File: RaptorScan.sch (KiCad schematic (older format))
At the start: 1 part

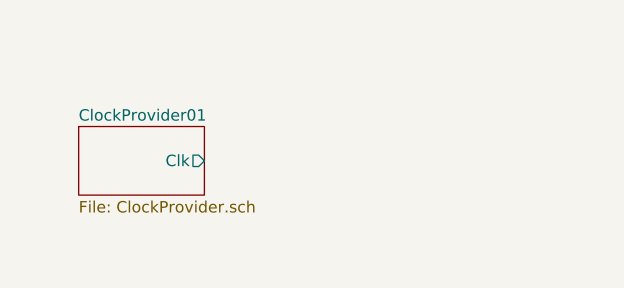
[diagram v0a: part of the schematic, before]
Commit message: Added: 7 Bit Counter
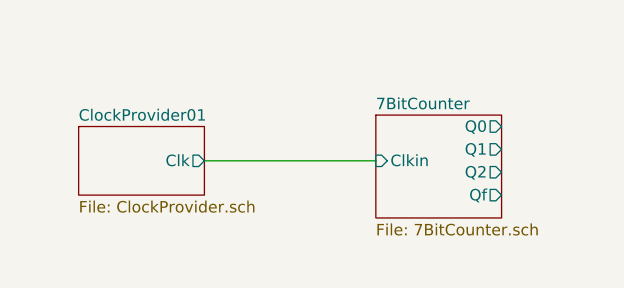
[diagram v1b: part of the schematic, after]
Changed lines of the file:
@@
 EESchema Schematic File Version 4
+LIBS:RaptorScan-cache
 EELAYER 29 0
 EELAYER END
 $Descr A4 11693 8268
 encoding utf-8
-Sheet 1 2
+Sheet 1 3
 Title ""
 Date ""
@@
 F0 "ClockProvider01" 50
 F1 "ClockProvider.sch" 50
-F4 "Clk" O R 2550 1100 50
+F2 "Clk" O R 2550 1100 50
 $EndSheet
 Wire Wire Line
@@
 	1    0    0    -1
 $EndComp
+$Sheet
+S 3300 900  550  450
+U 5D12D5A5
+F0 "7BitCounter" 50
+F1 "7BitCounter.sch" 50
+F2 "Clkin" I L 3300 1100 50
+F3 "Q0" O R 3850 950 50
+F4 "Q1" O R 3850 1050 50
+F5 "Q2" O R 3850 1150 50
+F6 "Qf" O R 3850 1250 50
+$EndSheet
+Wire Wire Line
+	2550 1100 3300 1100
 $EndSCHEMATC

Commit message: Update
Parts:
- added D1, D2, D3: LED, symbol Device:LED
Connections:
- net GND: now also D1.1 (K), D2.1 (K), D3.1 (K)
- new net MuxDecoder/A: D1.2 (A)
- new net MuxDecoder/B: D2.2 (A)
- new net MuxDecoder/C: D3.2 (A)
- no-connect marks 0 -> 4
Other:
- moved on the sheet: BT1
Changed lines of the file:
@@
 $Descr A4 11693 8268
 encoding utf-8
-Sheet 1 3
+Sheet 1 4
 Title ""
 Date ""
@@
 $EndDescr
 $Sheet
-S 2000 950  550  300
+S 2300 950  550  300
 U 5D1172DE
 F0 "ClockProvider01" 50
 F1 "ClockProvider.sch" 50
-F2 "Clk" O R 2550 1100 50
+F2 "Clk" O R 2850 1100 50
 $EndSheet
 Wire Wire Line
-	1100 700  1100 750
+	1500 800  1500 850
 $Comp
 L power:+12V #PWR0102
 U 1 1 5D1362F3
-P 1100 700
-F 0 "#PWR0102" H 1100 550 50  0001 C CNN
-F 1 "+12V" H 1115 873 50  0000 C CNN
-F 2 "" H 1100 700 50  0001 C CNN
-F 3 "" H 1100 700 50  0001 C CNN
-	1    1100 700
+P 1500 800
+F 0 "#PWR0102" H 1500 650 50  0001 C CNN
+F 1 "+12V" H 1515 973 50  0000 C CNN
+F 2 "" H 1500 800 50  0001 C CNN
+F 3 "" H 1500 800 50  0001 C CNN
+	1    1500 800
 	1    0    0    -1
 $EndComp
@@
 L power:GND #PWR0103
 U 1 1 5D137CC7
-P 1100 1350
-F 0 "#PWR0103" H 1100 1100 50  0001 C CNN
-F 1 "GND" H 1105 1177 50  0000 C CNN
-F 2 "" H 1100 1350 50  0001 C CNN
-F 3 "" H 1100 1350 50  0001 C CNN
-	1    1100 1350
-	1    0    0    -1
-$EndComp
-Wire Wire Line
-	1100 1250 1100 1300
+P 1500 1450
+F 0 "#PWR0103" H 1500 1200 50  0001 C CNN
+F 1 "GND" H 1505 1277 50  0000 C CNN
+F 2 "" H 1500 1450 50  0001 C CNN
+F 3 "" H 1500 1450 50  0001 C CNN
+	1    1500 1450
+	1    0    0    -1
+$EndComp
+Wire Wire Line
+	1500 1350 1500 1400
 $Comp
 L power:PWR_FLAG #FLG0101
 U 1 1 5D13C6DB
-P 1100 750
-F 0 "#FLG0101" H 1100 825 50  0001 C CNN
-F 1 "PWR_FLAG" V 1100 878 50  0000 L CNN
-F 2 "" H 1100 750 50  0001 C CNN
-F 3 "~" H 1100 750 50  0001 C CNN
-	1    1100 750
+P 1500 850
+F 0 "#FLG0101" H 1500 925 50  0001 C CNN
+F 1 "PWR_FLAG" V 1500 978 50  0000 L CNN
+F 2 "" H 1500 850 50  0001 C CNN
+F 3 "~" H 1500 850 50  0001 C CNN
+	1    1500 850
 	0    1    1    0
 $EndComp
-Connection ~ 1100 750
-Wire Wire Line
-	1100 750  1100 850
+Connection ~ 1500 850
+Wire Wire Line
+	1500 850  1500 950
 $Comp
 L power:PWR_FLAG #FLG0102
 U 1 1 5D13CBD4
-P 1100 1300
-F 0 "#FLG0102" H 1100 1375 50  0001 C CNN
-F 1 "PWR_FLAG" V 1100 1428 50  0000 L CNN
-F 2 "" H 1100 1300 50  0001 C CNN
-F 3 "~" H 1100 1300 50  0001 C CNN
-	1    1100 1300
+P 1500 1400
+F 0 "#FLG0102" H 1500 1475 50  0001 C CNN
+F 1 "PWR_FLAG" V 1500 1528 50  0000 L CNN
+F 2 "" H 1500 1400 50  0001 C CNN
+F 3 "~" H 1500 1400 50  0001 C CNN
+	1    1500 1400
 	0    1    1    0
 $EndComp
-Connection ~ 1100 1300
-Wire Wire Line
-	1100 1300 1100 1350
+Connection ~ 1500 1400
+Wire Wire Line
+	1500 1400 1500 1450
 $Comp
 L Device:Battery BT1
 U 1 1 5D11AF0F
-P 1100 1050
-F 0 "BT1" H 1208 1096 50  0000 L CNN
-F 1 "12V" H 1208 1005 50  0000 L CNN
-F 2 "" V 1100 1110 50  0001 C CNN
-F 3 "~" V 1100 1110 50  0001 C CNN
-	1    1100 1050
+P 1500 1150
+F 0 "BT1" H 1608 1196 50  0000 L CNN
+F 1 "12V" H 1608 1105 50  0000 L CNN
+F 2 "" V 1500 1210 50  0001 C CNN
+F 3 "~" V 1500 1210 50  0001 C CNN
+	1    1500 1150
 	1    0    0    -1
 $EndComp
 $Sheet
-S 3300 900  550  450
+S 4300 1050 550  700
 U 5D12D5A5
 F0 "7BitCounter" 50
 F1 "7BitCounter.sch" 50
-F2 "Clkin" I L 3300 1100 50
-F3 "Q0" O R 3850 950 50
-F4 "Q1" O R 3850 1050 50
-F5 "Q2" O R 3850 1150 50
-F6 "Qf" O R 3850 1250 50
+F2 "Clkin" I L 4300 1100 50
+F3 "Q0" O L 4300 1400 50
+F4 "Q1" O L 4300 1500 50
+F5 "Q2" O L 4300 1600 50
+F6 "Q3" O L 4300 1700 50
+F7 "Q4" O R 4850 1700 50
+F8 "Q5" O R 4850 1600 50
+F9 "Q6" O R 4850 1500 50
 $EndSheet
-Wire Wire Line
-	2550 1100 3300 1100
+$Sheet
+S 3200 1050 800  600
+U 5D12D28E
+F0 "MuxDecoder" 50
+F1 "MuxDecoder.sch" 50
+F2 "A" O L 3200 1400 50
+F3 "B" O L 3200 1500 50
+F4 "C" O L 3200 1600 50
+F5 "X" I R 4000 1400 50
+F6 "Y" I R 4000 1500 50
+F7 "Z" I R 4000 1600 50
+F8 "Clkin" I L 3200 1100 50
+F9 "ClkOut" O R 4000 1100 50
+$EndSheet
+Wire Wire Line
+	4300 1400 4000 1400
+Wire Wire Line
+	4300 1500 4000 1500
+Wire Wire Line
+	4300 1600 4000 1600
+NoConn ~ 4300 1700
+Wire Wire Line
+	2850 1100 3200 1100
+Wire Wire Line
+	4000 1100 4300 1100
+NoConn ~ 4850 1500
+NoConn ~ 4850 1600
+NoConn ~ 4850 1700
+$Comp
+L Device:LED D1
+U 1 1 5D23D3BD
+P 2550 1600
+F 0 "D1" H 2543 1816 50  0000 C CNN
+F 1 "LED" H 2543 1725 50  0000 C CNN
+F 2 "" H 2550 1600 50  0001 C CNN
+F 3 "~" H 2550 1600 50  0001 C CNN
+	1    2550 1600
+	1    0    0    -1
+$EndComp
+$Comp
+L Device:LED D2
+U 1 1 5D23E2F8
+P 2550 1950
+F 0 "D2" H 2543 2166 50  0000 C CNN
+F 1 "LED" H 2543 2075 50  0000 C CNN
+F 2 "" H 2550 1950 50  0001 C CNN
+F 3 "~" H 2550 1950 50  0001 C CNN
+	1    2550 1950
+	1    0    0    -1
+$EndComp
+$Comp
+L Device:LED D3
+U 1 1 5D23E6C2
+P 2550 2300
+F 0 "D3" H 2543 2516 50  0000 C CNN
+F 1 "LED" H 2543 2425 50  0000 C CNN
+F 2 "" H 2550 2300 50  0001 C CNN
+F 3 "~" H 2550 2300 50  0001 C CNN
+	1    2550 2300
+	1    0    0    -1
+$EndComp
+Wire Wire Line
+	2700 1600 2900 1600
+Wire Wire Line
+	2900 1600 2900 1400
+Wire Wire Line
+	2900 1400 3200 1400
+Wire Wire Line
+	3200 1500 3000 1500
+Wire Wire Line
+	3000 1500 3000 1950
+Wire Wire Line
+	3000 1950 2700 1950
+Wire Wire Line
+	3200 1600 3100 1600
+Wire Wire Line
+	3100 1600 3100 2300
+Wire Wire Line
+	3100 2300 2700 2300
+Wire Wire Line
+	2400 2300 2200 2300
+Wire Wire Line
+	2200 2300 2200 1950
+Wire Wire Line
+	2200 1600 2400 1600
+Wire Wire Line
+	2400 1950 2200 1950
+Connection ~ 2200 1950
+Wire Wire Line
+	2200 1950 2200 1600
+$Comp
+L power:GND #PWR0104
+U 1 1 5D23FAED
+P 2200 2300
+F 0 "#PWR0104" H 2200 2050 50  0001 C CNN
+F 1 "GND" H 2205 2127 50  0000 C CNN
+F 2 "" H 2200 2300 50  0001 C CNN
+F 3 "" H 2200 2300 50  0001 C CNN
+	1    2200 2300
+	1    0    0    -1
+$EndComp
+Connection ~ 2200 2300
 $EndSCHEMATC

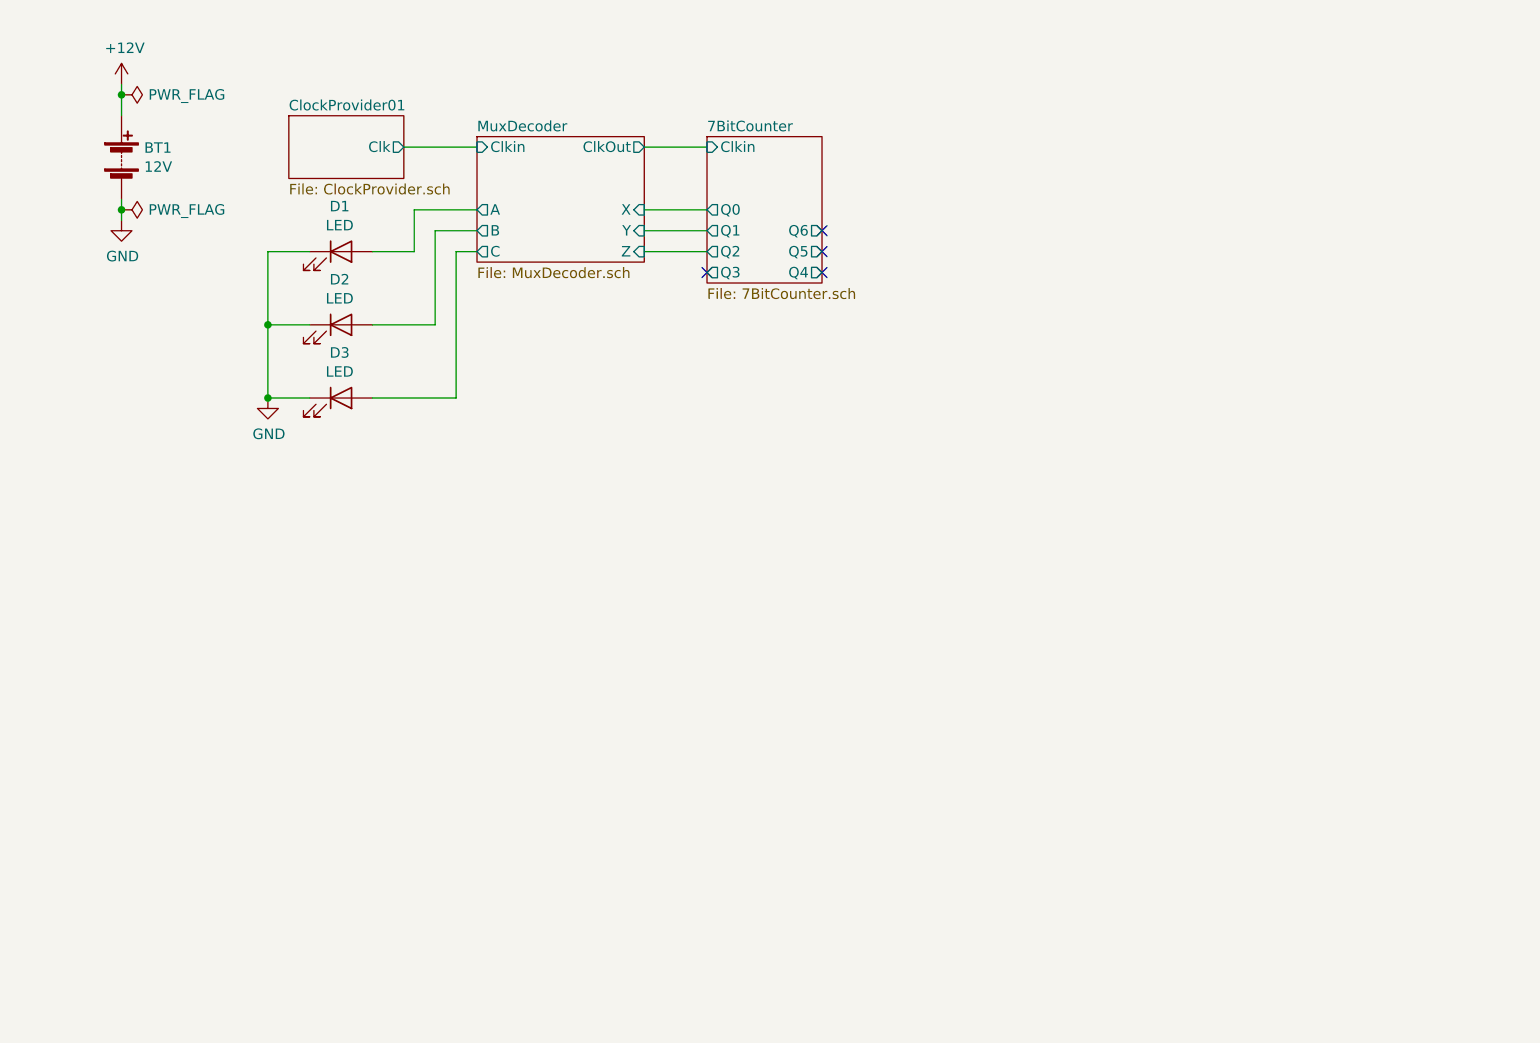
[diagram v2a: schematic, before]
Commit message: Added: connectors
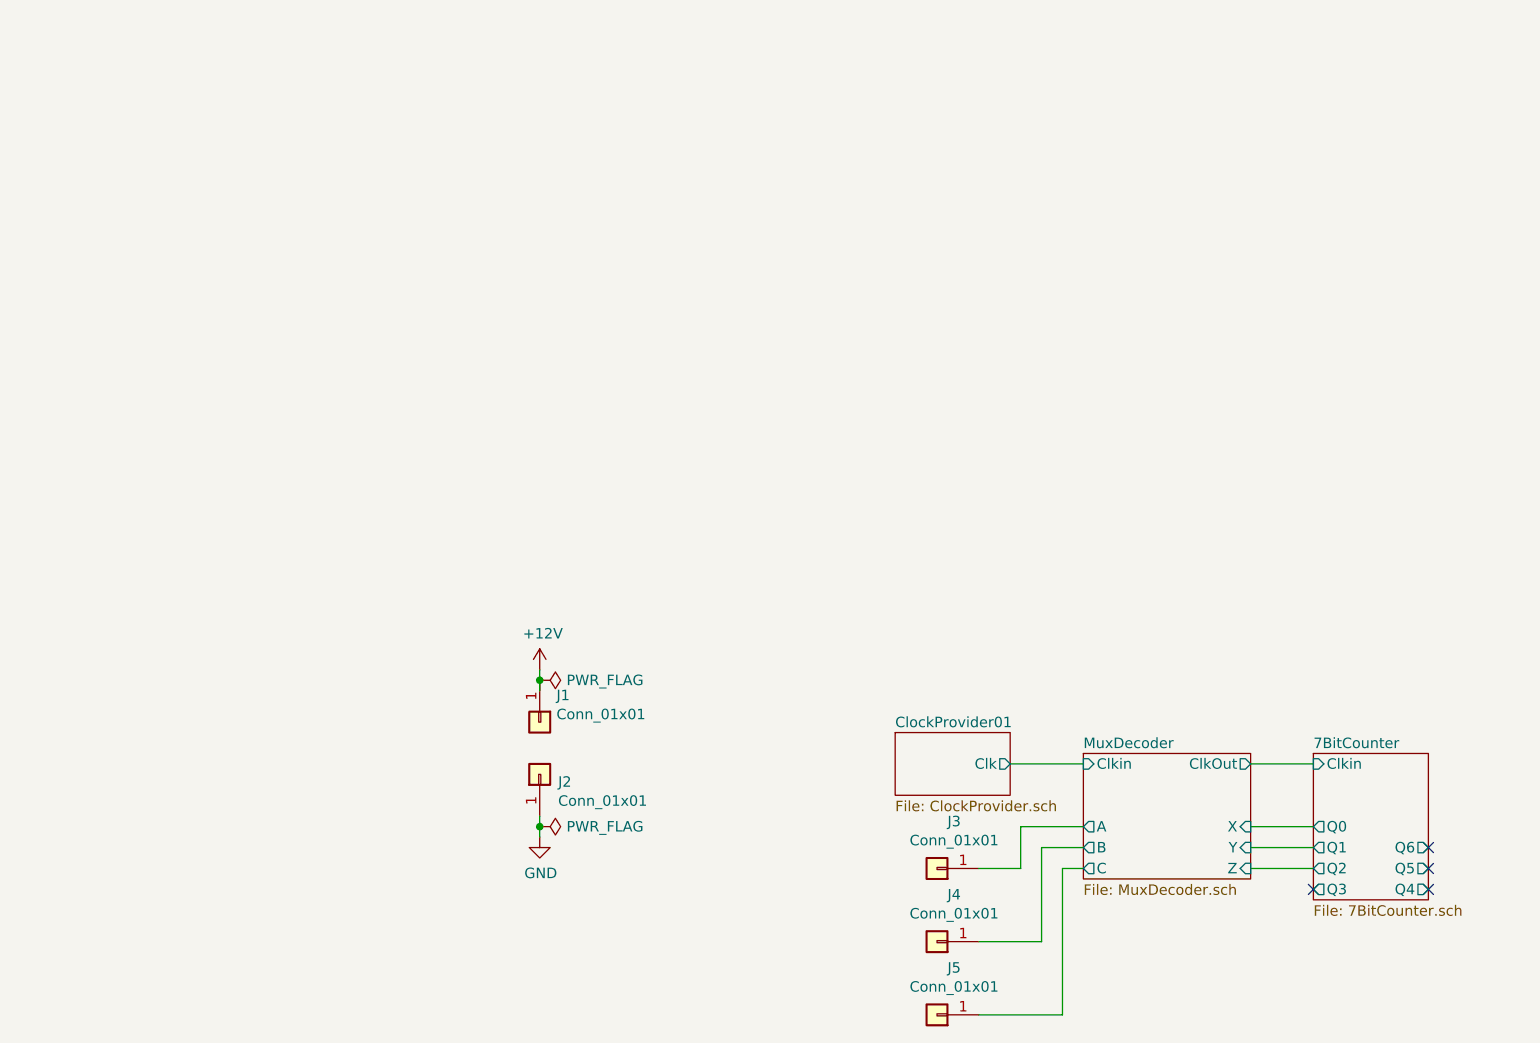
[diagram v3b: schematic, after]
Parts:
- removed BT1: 12V, symbol Device:Battery
- removed D1, D2, D3: LED, symbol Device:LED
- added J1, J2, J3, J4, J5: Conn_01x01, symbol Connector_Generic:Conn_01x01
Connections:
- wire segments 23 -> 18
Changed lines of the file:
@@
 $EndDescr
 $Sheet
-S 2300 950  550  300
+S 5200 3900 550  300
 U 5D1172DE
 F0 "ClockProvider01" 50
 F1 "ClockProvider.sch" 50
-F2 "Clk" O R 2850 1100 50
+F2 "Clk" O R 5750 4050 50
 $EndSheet
 Wire Wire Line
-	1500 800  1500 850
+	3500 3600 3500 3650
 $Comp
 L power:+12V #PWR0102
 U 1 1 5D1362F3
-P 1500 800
-F 0 "#PWR0102" H 1500 650 50  0001 C CNN
-F 1 "+12V" H 1515 973 50  0000 C CNN
-F 2 "" H 1500 800 50  0001 C CNN
-F 3 "" H 1500 800 50  0001 C CNN
-	1    1500 800
+P 3500 3600
+F 0 "#PWR0102" H 3500 3450 50  0001 C CNN
+F 1 "+12V" H 3515 3773 50  0000 C CNN
+F 2 "" H 3500 3600 50  0001 C CNN
+F 3 "" H 3500 3600 50  0001 C CNN
+	1    3500 3600
 	1    0    0    -1
 $EndComp
@@
 L power:GND #PWR0103
 U 1 1 5D137CC7
-P 1500 1450
-F 0 "#PWR0103" H 1500 1200 50  0001 C CNN
-F 1 "GND" H 1505 1277 50  0000 C CNN
-F 2 "" H 1500 1450 50  0001 C CNN
-F 3 "" H 1500 1450 50  0001 C CNN
-	1    1500 1450
+P 3500 4400
+F 0 "#PWR0103" H 3500 4150 50  0001 C CNN
+F 1 "GND" H 3505 4227 50  0000 C CNN
+F 2 "" H 3500 4400 50  0001 C CNN
+F 3 "" H 3500 4400 50  0001 C CNN
+	1    3500 4400
 	1    0    0    -1
 $EndComp
 Wire Wire Line
-	1500 1350 1500 1400
+	3500 4300 3500 4350
 $Comp
 L power:PWR_FLAG #FLG0101
 U 1 1 5D13C6DB
-P 1500 850
-F 0 "#FLG0101" H 1500 925 50  0001 C CNN
-F 1 "PWR_FLAG" V 1500 978 50  0000 L CNN
-F 2 "" H 1500 850 50  0001 C CNN
-F 3 "~" H 1500 850 50  0001 C CNN
-	1    1500 850
+P 3500 3650
+F 0 "#FLG0101" H 3500 3725 50  0001 C CNN
+F 1 "PWR_FLAG" V 3500 3778 50  0000 L CNN
+F 2 "" H 3500 3650 50  0001 C CNN
+F 3 "~" H 3500 3650 50  0001 C CNN
+	1    3500 3650
 	0    1    1    0
 $EndComp
-Connection ~ 1500 850
+Connection ~ 3500 3650
 Wire Wire Line
-	1500 850  1500 950
+	3500 3650 3500 3700
 $Comp
 L power:PWR_FLAG #FLG0102
 U 1 1 5D13CBD4
-P 1500 1400
-F 0 "#FLG0102" H 1500 1475 50  0001 C CNN
-F 1 "PWR_FLAG" V 1500 1528 50  0000 L CNN
-F 2 "" H 1500 1400 50  0001 C CNN
-F 3 "~" H 1500 1400 50  0001 C CNN
-	1    1500 1400
+P 3500 4350
+F 0 "#FLG0102" H 3500 4425 50  0001 C CNN
+F 1 "PWR_FLAG" V 3500 4478 50  0000 L CNN
+F 2 "" H 3500 4350 50  0001 C CNN
+F 3 "~" H 3500 4350 50  0001 C CNN
+	1    3500 4350
 	0    1    1    0
 $EndComp
-Connection ~ 1500 1400
+Connection ~ 3500 4350
 Wire Wire Line
-	1500 1400 1500 1450
-$Comp
-L Device:Battery BT1
-U 1 1 5D11AF0F
-P 1500 1150
-F 0 "BT1" H 1608 1196 50  0000 L CNN
-F 1 "12V" H 1608 1105 50  0000 L CNN
-F 2 "" V 1500 1210 50  0001 C CNN
-F 3 "~" V 1500 1210 50  0001 C CNN
-	1    1500 1150
-	1    0    0    -1
-$EndComp
+	3500 4350 3500 4400
 $Sheet
-S 4300 1050 550  700
+S 7200 4000 550  700
 U 5D12D5A5
 F0 "7BitCounter" 50
 F1 "7BitCounter.sch" 50
-F2 "Clkin" I L 4300 1100 50
-F3 "Q0" O L 4300 1400 50
-F4 "Q1" O L 4300 1500 50
-F5 "Q2" O L 4300 1600 50
-F6 "Q3" O L 4300 1700 50
-F7 "Q4" O R 4850 1700 50
-F8 "Q5" O R 4850 1600 50
-F9 "Q6" O R 4850 1500 50
+F2 "Clkin" I L 7200 4050 50
+F3 "Q0" O L 7200 4350 50
+F4 "Q1" O L 7200 4450 50
+F5 "Q2" O L 7200 4550 50
+F6 "Q3" O L 7200 4650 50
+F7 "Q4" O R 7750 4650 50
+F8 "Q5" O R 7750 4550 50
+F9 "Q6" O R 7750 4450 50
 $EndSheet
 $Sheet
-S 3200 1050 800  600
+S 6100 4000 800  600
 U 5D12D28E
 F0 "MuxDecoder" 50
 F1 "MuxDecoder.sch" 50
-F2 "A" O L 3200 1400 50
-F3 "B" O L 3200 1500 50
-F4 "C" O L 3200 1600 50
-F5 "X" I R 4000 1400 50
-F6 "Y" I R 4000 1500 50
-F7 "Z" I R 4000 1600 50
-F8 "Clkin" I L 3200 1100 50
-F9 "ClkOut" O R 4000 1100 50
+F2 "A" O L 6100 4350 50
+F3 "B" O L 6100 4450 50
+F4 "C" O L 6100 4550 50
+F5 "X" I R 6900 4350 50
+F6 "Y" I R 6900 4450 50
+F7 "Z" I R 6900 4550 50
+F8 "Clkin" I L 6100 4050 50
+F9 "ClkOut" O R 6900 4050 50
 $EndSheet
 Wire Wire Line
-	4300 1400 4000 1400
+	7200 4350 6900 4350
 Wire Wire Line
-	4300 1500 4000 1500
+	7200 4450 6900 4450
 Wire Wire Line
-	4300 1600 4000 1600
-NoConn ~ 4300 1700
+	7200 4550 6900 4550
+NoConn ~ 7200 4650
 Wire Wire Line
-	2850 1100 3200 1100
+	5750 4050 6100 4050
 Wire Wire Line
-	4000 1100 4300 1100
-NoConn ~ 4850 1500
-NoConn ~ 4850 1600
-NoConn ~ 4850 1700
+	6900 4050 7200 4050
+NoConn ~ 7750 4450
+NoConn ~ 7750 4550
+NoConn ~ 7750 4650
+Wire Wire Line
+	5600 4550 5800 4550
+Wire Wire Line
+	5800 4550 5800 4350
+Wire Wire Line
+	5800 4350 6100 4350
+Wire Wire Line
+	6100 4450 5900 4450
+Wire Wire Line
+	5900 4450 5900 4900
+Wire Wire Line
+	5900 4900 5600 4900
+Wire Wire Line
+	6100 4550 6000 4550
+Wire Wire Line
+	6000 4550 6000 5250
+Wire Wire Line
+	6000 5250 5600 5250
 $Comp
-L Device:LED D1
-U 1 1 5D23D3BD
-P 2550 1600
-F 0 "D1" H 2543 1816 50  0000 C CNN
-F 1 "LED" H 2543 1725 50  0000 C CNN
-F 2 "" H 2550 1600 50  0001 C CNN
-F 3 "~" H 2550 1600 50  0001 C CNN
-	1    2550 1600
-	1    0    0    -1
+L Connector_Generic:Conn_01x01 J1
+U 1 1 5D13F6A9
+P 3500 3850
+F 0 "J1" V 3372 3930 50  0000 L CNN
+F 1 "Conn_01x01" V 3463 3930 50  0000 L CNN
+F 2 "" H 3500 3850 50  0001 C CNN
+F 3 "~" H 3500 3850 50  0001 C CNN
+	1    3500 3850
+	0    1    1    0
 $EndComp
 $Comp
-L Device:LED D2
-U 1 1 5D23E2F8
-P 2550 1950
-F 0 "D2" H 2543 2166 50  0000 C CNN
-F 1 "LED" H 2543 2075 50  0000 C CNN
-F 2 "" H 2550 1950 50  0001 C CNN
-F 3 "~" H 2550 1950 50  0001 C CNN
-	1    2550 1950
-	1    0    0    -1
+L Connector_Generic:Conn_01x01 J2
+U 1 1 5D14070D
+P 3500 4100
+F 0 "J2" V 3464 4012 50  0000 R CNN
+F 1 "Conn_01x01" V 3373 4012 50  0000 R CNN
+F 2 "" H 3500 4100 50  0001 C CNN
+F 3 "~" H 3500 4100 50  0001 C CNN
+	1    3500 4100
+	0    -1   -1   0
 $EndComp
 $Comp
-L Device:LED D3
-U 1 1 5D23E6C2
-P 2550 2300
-F 0 "D3" H 2543 2516 50  0000 C CNN
-F 1 "LED" H 2543 2425 50  0000 C CNN
-F 2 "" H 2550 2300 50  0001 C CNN
-F 3 "~" H 2550 2300 50  0001 C CNN
-	1    2550 2300
-	1    0    0    -1
+L Connector_Generic:Conn_01x01 J3
+U 1 1 5D145A5E
+P 5400 4550
+F 0 "J3" H 5318 4325 50  0000 C CNN
+F 1 "Conn_01x01" H 5318 4416 50  0000 C CNN
+F 2 "" H 5400 4550 50  0001 C CNN
+F 3 "~" H 5400 4550 50  0001 C CNN
+	1    5400 4550
+	-1   0    0    1
 $EndComp
-Wire Wire Line
-	2700 1600 2900 1600
-Wire Wire Line
-	2900 1600 2900 1400
-Wire Wire Line
-	2900 1400 3200 1400
-Wire Wire Line
-	3200 1500 3000 1500
-Wire Wire Line
-	3000 1500 3000 1950
-Wire Wire Line
-	3000 1950 2700 1950
-Wire Wire Line
-	3200 1600 3100 1600
-Wire Wire Line
-	3100 1600 3100 2300
-Wire Wire Line
-	3100 2300 2700 2300
-Wire Wire Line
-	2400 2300 2200 2300
-Wire Wire Line
-	2200 2300 2200 1950
-Wire Wire Line
-	2200 1600 2400 1600
-Wire Wire Line
-	2400 1950 2200 1950
-Connection ~ 2200 1950
-Wire Wire Line
-	2200 1950 2200 1600
 $Comp
-L power:GND #PWR0104
-U 1 1 5D23FAED
-P 2200 2300
-F 0 "#PWR0104" H 2200 2050 50  0001 C CNN
-F 1 "GND" H 2205 2127 50  0000 C CNN
-F 2 "" H 2200 2300 50  0001 C CNN
-F 3 "" H 2200 2300 50  0001 C CNN
-	1    2200 2300
-	1    0    0    -1
+L Connector_Generic:Conn_01x01 J4
+U 1 1 5D146214
+P 5400 4900
+F 0 "J4" H 5318 4675 50  0000 C CNN
+F 1 "Conn_01x01" H 5318 4766 50  0000 C CNN
+F 2 "" H 5400 4900 50  0001 C CNN
+F 3 "~" H 5400 4900 50  0001 C CNN
+	1    5400 4900
+	-1   0    0    1
 $EndComp
-Connection ~ 2200 2300
+$Comp
+L Connector_Generic:Conn_01x01 J5
+U 1 1 5D1464E8
+P 5400 5250
+F 0 "J5" H 5318 5025 50  0000 C CNN
+F 1 "Conn_01x01" H 5318 5116 50  0000 C CNN
+F 2 "" H 5400 5250 50  0001 C CNN
+F 3 "~" H 5400 5250 50  0001 C CNN
+	1    5400 5250
+	-1   0    0    1
+$EndComp
 $EndSCHEMATC

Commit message: Added: pcb
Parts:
- J1, J2, J3, J4, J5: footprint (none) -> Connector_PinHeader_2.54mm:PinHeader_1x01_P2.54mm_Vertical
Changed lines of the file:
@@
 F 0 "J1" V 3372 3930 50  0000 L CNN
 F 1 "Conn_01x01" V 3463 3930 50  0000 L CNN
-F 2 "" H 3500 3850 50  0001 C CNN
+F 2 "Connector_PinHeader_2.54mm:PinHeader_1x01_P2.54mm_Vertical" H 3500 3850 50  0001 C CNN
 F 3 "~" H 3500 3850 50  0001 C CNN
 	1    3500 3850
@@
 F 0 "J2" V 3464 4012 50  0000 R CNN
 F 1 "Conn_01x01" V 3373 4012 50  0000 R CNN
-F 2 "" H 3500 4100 50  0001 C CNN
+F 2 "Connector_PinHeader_2.54mm:PinHeader_1x01_P2.54mm_Vertical" H 3500 4100 50  0001 C CNN
 F 3 "~" H 3500 4100 50  0001 C CNN
 	1    3500 4100
@@
 F 0 "J3" H 5318 4325 50  0000 C CNN
 F 1 "Conn_01x01" H 5318 4416 50  0000 C CNN
-F 2 "" H 5400 4550 50  0001 C CNN
+F 2 "Connector_PinHeader_2.54mm:PinHeader_1x01_P2.54mm_Vertical" H 5400 4550 50  0001 C CNN
 F 3 "~" H 5400 4550 50  0001 C CNN
 	1    5400 4550
@@
 F 0 "J4" H 5318 4675 50  0000 C CNN
 F 1 "Conn_01x01" H 5318 4766 50  0000 C CNN
-F 2 "" H 5400 4900 50  0001 C CNN
+F 2 "Connector_PinHeader_2.54mm:PinHeader_1x01_P2.54mm_Vertical" H 5400 4900 50  0001 C CNN
 F 3 "~" H 5400 4900 50  0001 C CNN
 	1    5400 4900
@@
 F 0 "J5" H 5318 5025 50  0000 C CNN
 F 1 "Conn_01x01" H 5318 5116 50  0000 C CNN
-F 2 "" H 5400 5250 50  0001 C CNN
+F 2 "Connector_PinHeader_2.54mm:PinHeader_1x01_P2.54mm_Vertical" H 5400 5250 50  0001 C CNN
 F 3 "~" H 5400 5250 50  0001 C CNN
 	1    5400 5250
